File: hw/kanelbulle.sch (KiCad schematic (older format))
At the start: 1 part

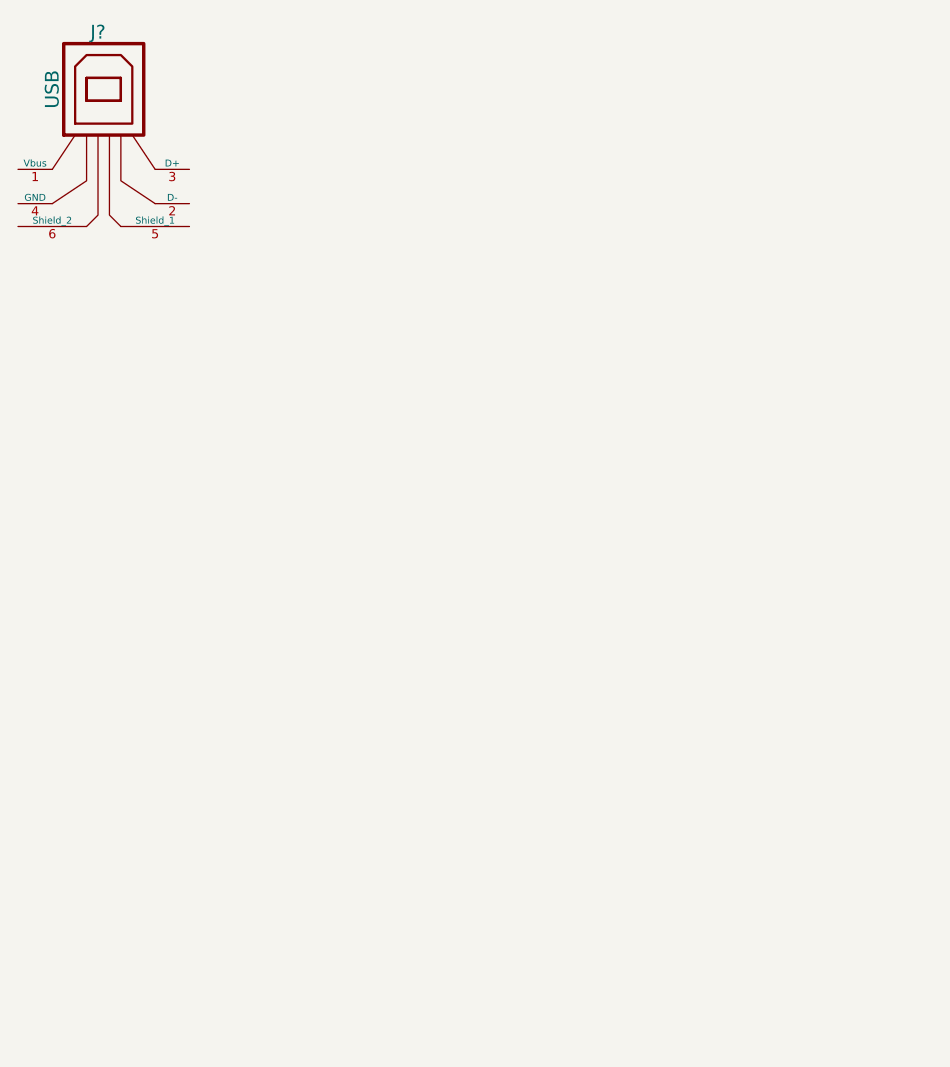
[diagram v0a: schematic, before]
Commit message: added micro controller to schematic
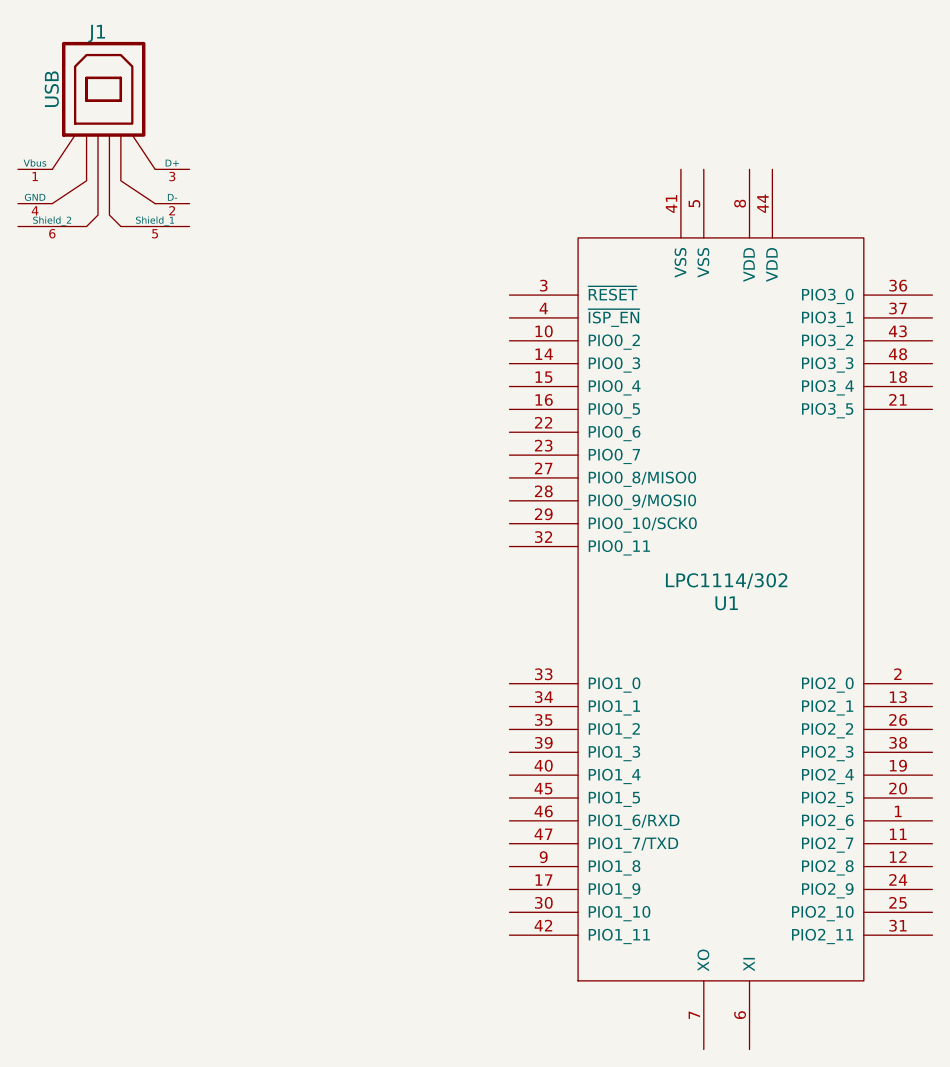
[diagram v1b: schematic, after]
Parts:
- added U1: LPC1114/302, symbol LPC1114/302
- gave numbers to parts that had none: 1
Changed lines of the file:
@@
 LIBS:contrib
 LIBS:valves
+LIBS:LPC1114
+LIBS:kanelbulle-cache
 EELAYER 27 0
 EELAYER END
@@
 $EndDescr
 $Comp
-L USB J?
+L USB J1
 U 1 1 54C8D9E1
 P 3150 1900
-F 0 "J?" H 3100 2300 60  0000 C CNN
+F 0 "J1" H 3100 2300 60  0000 C CNN
 F 1 "USB" V 2900 2050 60  0000 C CNN
 F 2 "" H 3150 1900 60  0000 C CNN
@@
 	1    0    0    -1
 $EndComp
+$Comp
+L LPC1114/302 U1
+U 1 1 54C8DD37
+P 5850 4050
+F 0 "U1" H 5850 4100 60  0000 C CNN
+F 1 "LPC1114/302" H 5850 4200 60  0000 C CNN
+F 2 "" H 5850 4050 60  0000 C CNN
+F 3 "" H 5850 4050 60  0000 C CNN
+	1    5850 4050
+	1    0    0    -1
+$EndComp

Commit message: leds, leds everywhere
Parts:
- added D1, D10, D11, D12, D13, D14, D15, D16, D17, D18, D19, D2, D20, D21, D22, D23, D24, D25, D26, D27, D28, D29, D3, D30, D31, D32, D33, D34, D35, D36, D37, D38, D39, D4, D40, D41, D42, D43, D44, D45, D46, D47, D48, D49, D5, D50, D51, D6, D7, D8, D9: LED_RGB, symbol LED_RGB

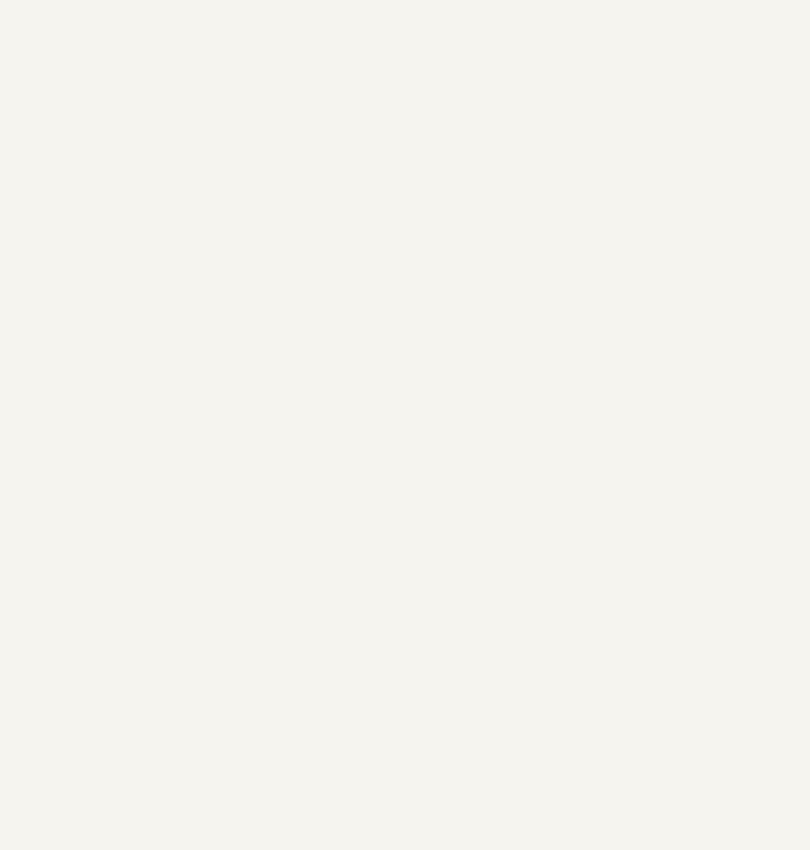
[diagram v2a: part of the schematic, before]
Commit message: added led driver chip
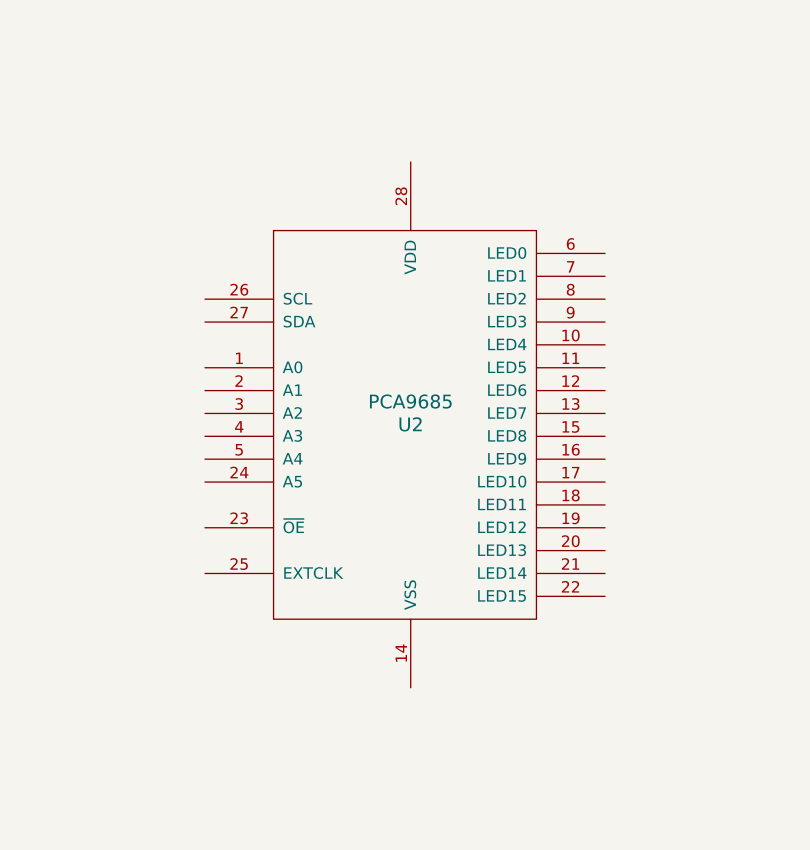
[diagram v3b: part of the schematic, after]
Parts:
- added U2: PCA9685, ~, symbol PCA9685
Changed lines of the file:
@@
 LIBS:LPC1114
 LIBS:led_rgb
+LIBS:pca9685
 LIBS:kanelbulle-cache
 EELAYER 27 0
@@
 	0    -1   -1   0
 $EndComp
+$Comp
+L PCA9685 U2
+U 1 1 54C91061
+P 12950 9250
+F 0 "U2" H 12950 9200 60  0000 C CNN
+F 1 "PCA9685" H 12950 9300 60  0000 C CNN
+F 2 "~" H 13500 8000 60  0000 C CNN
+F 3 "~" H 13500 8000 60  0000 C CNN
+	1    12950 9250
+	1    0    0    -1
+$EndComp
 $EndSCHEMATC

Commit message: connected leds on schematic
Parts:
- added R1, R10, R11, R12, R13, R14, R15, R16, R17, R18, R19, R2, R3, R4, R5, R6, R7, R8, R9: R, ~, symbol R
- added U3, U4, U5: ULN2003A, symbol ULN2003A
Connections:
- net labels added: 3V3, B1, B2, B3, B4, B5, G1, G2, G3, G4, G5, GND, R1, R2, R3, R4, R5, SCL, SDA
- wire segments 0 -> 315
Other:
- moved on the sheet: U2

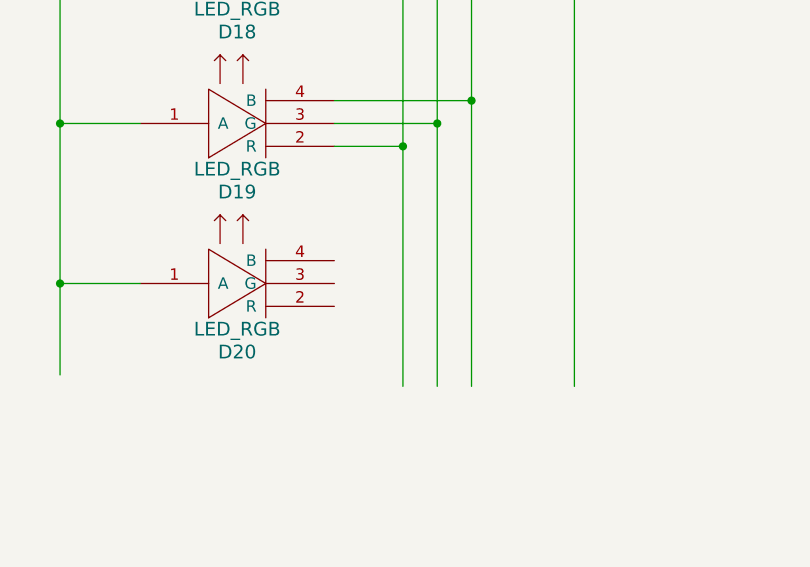
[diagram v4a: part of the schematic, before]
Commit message: connected leds to eachother
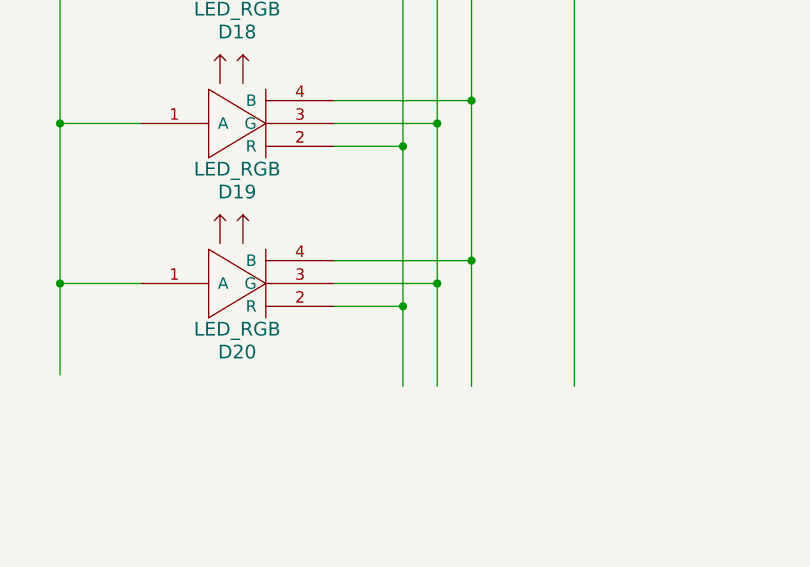
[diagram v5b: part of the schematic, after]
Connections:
- wire segments 315 -> 318
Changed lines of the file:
@@
 Wire Wire Line
 	13900 19200 13750 19200
+Wire Wire Line
+	21300 16400 21900 16400
+Connection ~ 21900 16400
+Wire Wire Line
+	21300 16500 21750 16500
+Connection ~ 21750 16500
+Wire Wire Line
+	21300 16600 21600 16600
+Connection ~ 21600 16600
 $EndSCHEMATC

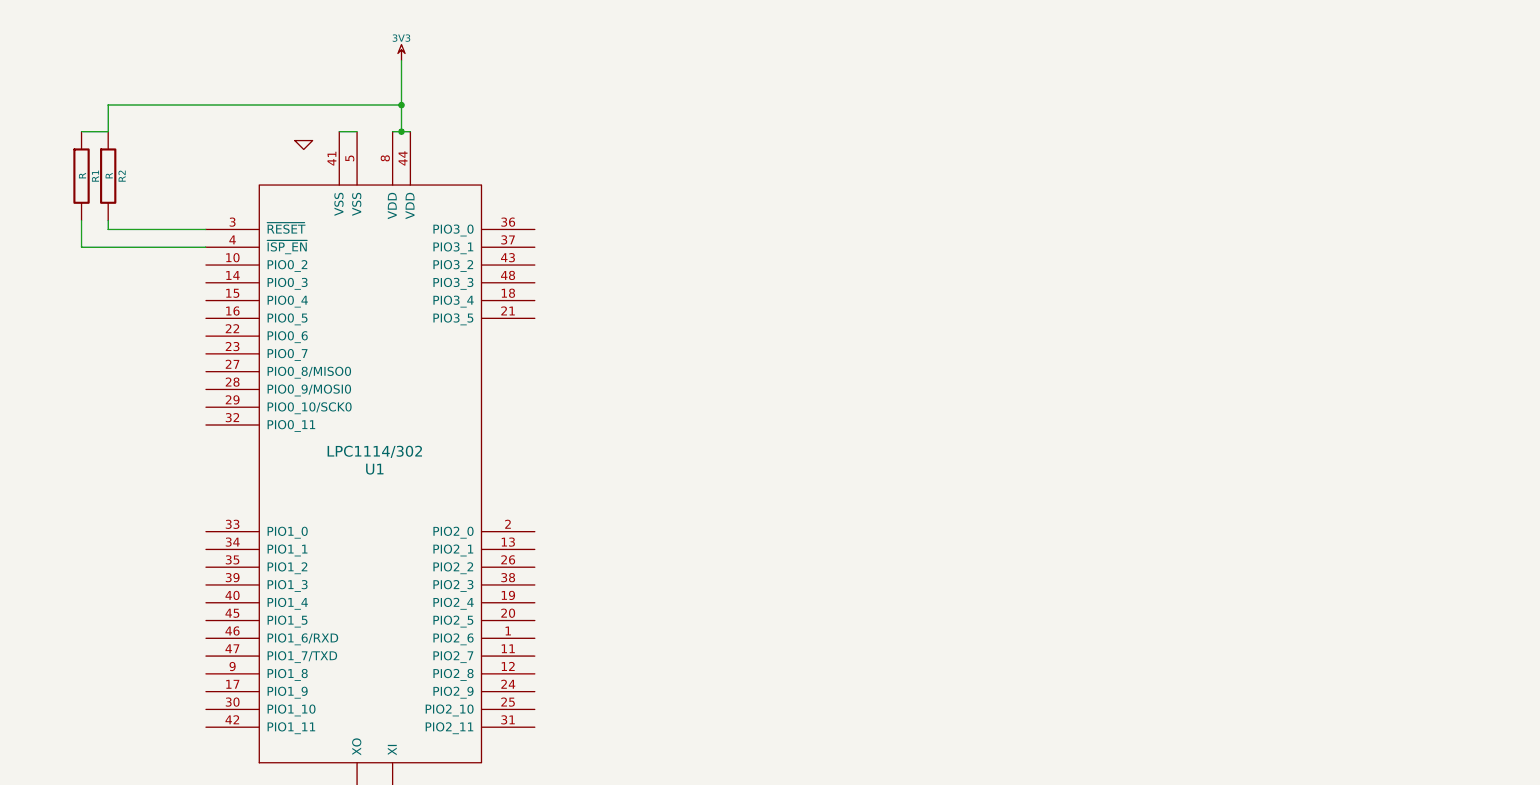
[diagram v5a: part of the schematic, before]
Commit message: connected some OC drivers
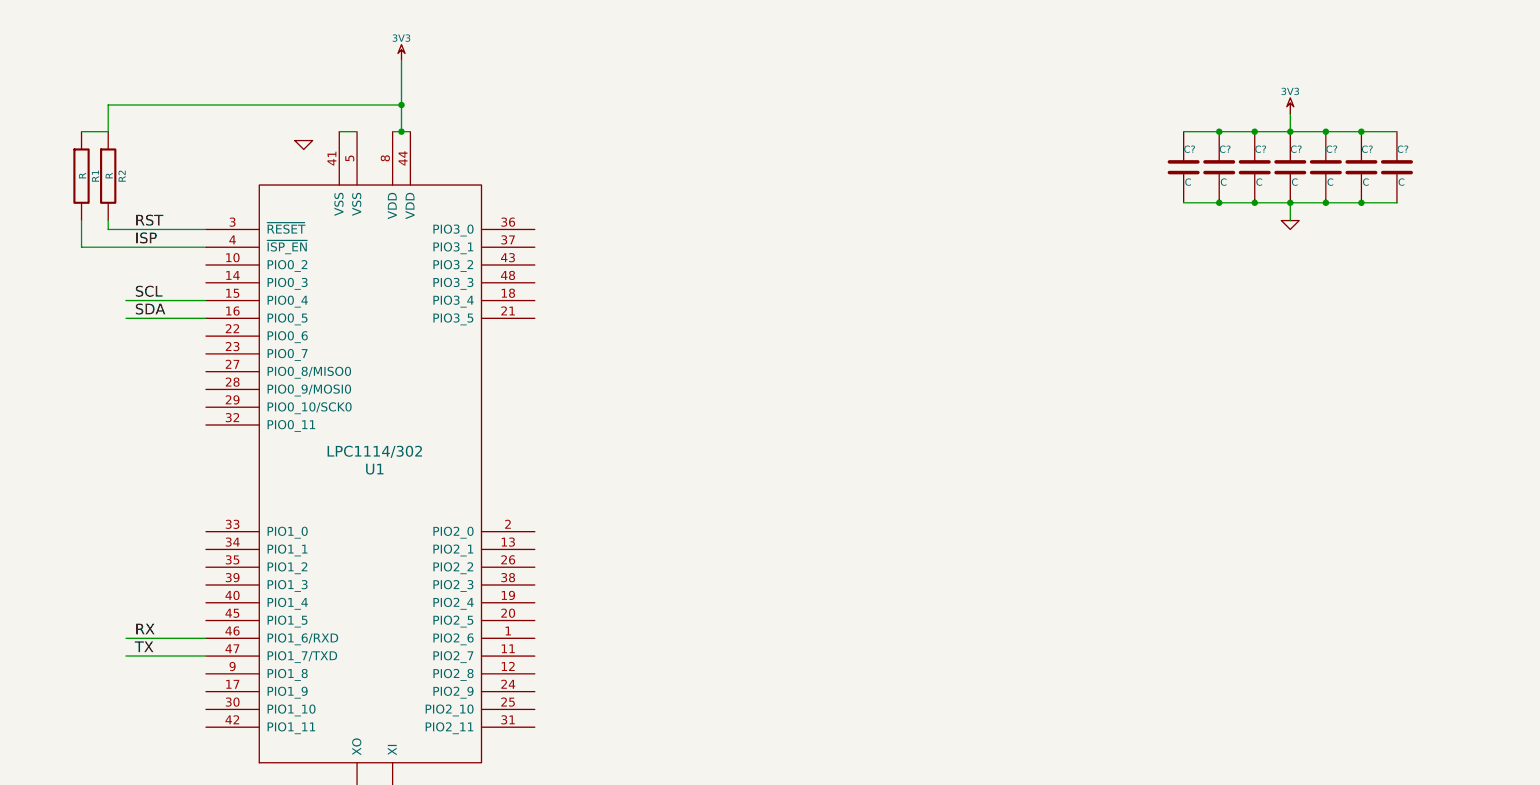
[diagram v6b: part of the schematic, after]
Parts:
- added C? (x7): C, ~, symbol C
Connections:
- net labels added: ISP, RST, RX, TX
- wire segments 318 -> 326
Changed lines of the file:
@@
 	11700 18500 10600 18500
 $Comp
-L 3V3 #PWR5
+L 3V3 #PWR01
 U 1 1 54CFB406
 P 20100 2350
-F 0 "#PWR5" H 20100 2450 40  0001 C CNN
+F 0 "#PWR01" H 20100 2450 40  0001 C CNN
 F 1 "3V3" H 20100 2475 40  0000 C CNN
 F 2 "" H 20100 2350 60  0000 C CNN
@@
 $EndComp
 $Comp
-L 3V3 #PWR6
+L 3V3 #PWR02
 U 1 1 54CFB413
 P 22350 2350
-F 0 "#PWR6" H 22350 2450 40  0001 C CNN
+F 0 "#PWR02" H 22350 2450 40  0001 C CNN
 F 1 "3V3" H 22350 2475 40  0000 C CNN
 F 2 "" H 22350 2350 60  0000 C CNN
@@
 $EndComp
 $Comp
-L 3V3 #PWR7
+L 3V3 #PWR03
 U 1 1 54CFB419
 P 24250 2350
-F 0 "#PWR7" H 24250 2450 40  0001 C CNN
+F 0 "#PWR03" H 24250 2450 40  0001 C CNN
 F 1 "3V3" H 24250 2475 40  0000 C CNN
 F 2 "" H 24250 2350 60  0000 C CNN
@@
 $EndComp
 $Comp
-L 3V3 #PWR8
+L 3V3 #PWR04
 U 1 1 54CFB41F
 P 26100 2350
-F 0 "#PWR8" H 26100 2450 40  0001 C CNN
+F 0 "#PWR04" H 26100 2450 40  0001 C CNN
 F 1 "3V3" H 26100 2475 40  0000 C CNN
 F 2 "" H 26100 2350 60  0000 C CNN
@@
 $EndComp
 $Comp
-L 3V3 #PWR9
+L 3V3 #PWR05
 U 1 1 54CFB425
 P 28050 2350
-F 0 "#PWR9" H 28050 2450 40  0001 C CNN
+F 0 "#PWR05" H 28050 2450 40  0001 C CNN
 F 1 "3V3" H 28050 2475 40  0000 C CNN
 F 2 "" H 28050 2350 60  0000 C CNN
@@
 Connection ~ 8150 16800
 $Comp
-L 3V3 #PWR3
+L 3V3 #PWR06
 U 1 1 54CFC851
 P 8150 16650
-F 0 "#PWR3" H 8150 16750 40  0001 C CNN
+F 0 "#PWR06" H 8150 16750 40  0001 C CNN
 F 1 "3V3" H 8150 16775 40  0000 C CNN
 F 2 "" H 8150 16650 60  0000 C CNN
@@
 $EndComp
 $Comp
-L GND #PWR4
+L GND #PWR07
 U 1 1 54CFC924
 P 8750 19100
-F 0 "#PWR4" H 8750 19100 30  0001 C CNN
+F 0 "#PWR07" H 8750 19100 30  0001 C CNN
 F 1 "GND" H 8750 19030 30  0001 C CNN
 F 2 "" H 8750 19100 60  0000 C CNN
@@
 	5950 2100 6050 2100
 $Comp
-L GND #PWR1
+L GND #PWR08
 U 1 1 54CFDFE0
 P 5450 2150
-F 0 "#PWR1" H 5450 2150 30  0001 C CNN
+F 0 "#PWR08" H 5450 2150 30  0001 C CNN
 F 1 "GND" H 5450 2080 30  0001 C CNN
 F 2 "" H 5450 2150 60  0000 C CNN
@@
 $EndComp
 $Comp
-L 3V3 #PWR2
+L 3V3 #PWR09
 U 1 1 54CFDFEF
 P 6000 1700
-F 0 "#PWR2" H 6000 1800 40  0001 C CNN
+F 0 "#PWR09" H 6000 1800 40  0001 C CNN
 F 1 "3V3" H 6000 1825 40  0000 C CNN
 F 2 "" H 6000 1700 60  0000 C CNN
@@
 	21300 16600 21600 16600
 Connection ~ 21600 16600
+Wire Wire Line
+	4900 3050 4450 3050
+Wire Wire Line
+	4900 3150 4450 3150
+Text Label 4500 3050 0    60   ~ 0
+SCL
+Text Label 4500 3150 0    60   ~ 0
+SDA
+Text Label 4500 2650 0    60   ~ 0
+RST
+Text Label 4500 2750 0    60   ~ 0
+ISP
+Wire Wire Line
+	4900 4950 4450 4950
+Wire Wire Line
+	4900 5050 4450 5050
+Text Label 4500 4950 0    60   ~ 0
+RX
+Text Label 4500 5050 0    60   ~ 0
+TX
+$Comp
+L C C?
+U 1 1 54CFB5F9
+P 10600 2300
+F 0 "C?" H 10600 2400 40  0000 L CNN
+F 1 "C" H 10606 2215 40  0000 L CNN
+F 2 "~" H 10638 2150 30  0000 C CNN
+F 3 "~" H 10600 2300 60  0000 C CNN
+	1    10600 2300
+	1    0    0    -1
+$EndComp
+$Comp
+L C C?
+U 1 1 54CFB606
+P 10800 2300
+F 0 "C?" H 10800 2400 40  0000 L CNN
+F 1 "C" H 10806 2215 40  0000 L CNN
+F 2 "~" H 10838 2150 30  0000 C CNN
+F 3 "~" H 10800 2300 60  0000 C CNN
+	1    10800 2300
+	1    0    0    -1
+$EndComp
+$Comp
+L C C?
+U 1 1 54CFB60C
+P 11000 2300
+F 0 "C?" H 11000 2400 40  0000 L CNN
+F 1 "C" H 11006 2215 40  0000 L CNN
+F 2 "~" H 11038 2150 30  0000 C CNN
+F 3 "~" H 11000 2300 60  0000 C CNN
+	1    11000 2300
+	1    0    0    -1
+$EndComp
+$Comp
+L C C?
+U 1 1 54CFB612
+P 11200 2300
+F 0 "C?" H 11200 2400 40  0000 L CNN
+F 1 "C" H 11206 2215 40  0000 L CNN
+F 2 "~" H 11238 2150 30  0000 C CNN
+F 3 "~" H 11200 2300 60  0000 C CNN
+	1    11200 2300
+	1    0    0    -1
+$EndComp
+$Comp
+L C C?
+U 1 1 54CFB618
+P 11400 2300
+F 0 "C?" H 11400 2400 40  0000 L CNN
+F 1 "C" H 11406 2215 40  0000 L CNN
+F 2 "~" H 11438 2150 30  0000 C CNN
+F 3 "~" H 11400 2300 60  0000 C CNN
+	1    11400 2300
+	1    0    0    -1
+$EndComp
+$Comp
+L C C?
+U 1 1 54CFB61E
+P 11600 2300
+F 0 "C?" H 11600 2400 40  0000 L CNN
+F 1 "C" H 11606 2215 40  0000 L CNN
+F 2 "~" H 11638 2150 30  0000 C CNN
+F 3 "~" H 11600 2300 60  0000 C CNN
+	1    11600 2300
+	1    0    0    -1
+$EndComp
+$Comp
+L C C?
+U 1 1 54CFB624
+P 10400 2300
+F 0 "C?" H 10400 2400 40  0000 L CNN
+F 1 "C" H 10406 2215 40  0000 L CNN
+F 2 "~" H 10438 2150 30  0000 C CNN
+F 3 "~" H 10400 2300 60  0000 C CNN
+	1    10400 2300
+	1    0    0    -1
+$EndComp
+Wire Wire Line
+	10400 2100 11600 2100
+Connection ~ 10600 2100
+Connection ~ 10800 2100
+Connection ~ 11000 2100
+Connection ~ 11200 2100
+Connection ~ 11400 2100
+Wire Wire Line
+	10400 2500 11600 2500
+Connection ~ 10600 2500
+Connection ~ 10800 2500
+Connection ~ 11000 2500
+Connection ~ 11200 2500
+Connection ~ 11400 2500
+$Comp
+L GND #PWR?
+U 1 1 54CFCF5E
+P 11000 2600
+F 0 "#PWR?" H 11000 2600 30  0001 C CNN
+F 1 "GND" H 11000 2530 30  0001 C CNN
+F 2 "" H 11000 2600 60  0000 C CNN
+F 3 "" H 11000 2600 60  0000 C CNN
+	1    11000 2600
+	1    0    0    -1
+$EndComp
+Wire Wire Line
+	11000 2600 11000 2500
+$Comp
+L 3V3 #PWR?
+U 1 1 54CFD18D
+P 11000 2000
+F 0 "#PWR?" H 11000 2100 40  0001 C CNN
+F 1 "3V3" H 11000 2125 40  0000 C CNN
+F 2 "" H 11000 2000 60  0000 C CNN
+F 3 "" H 11000 2000 60  0000 C CNN
+	1    11000 2000
+	1    0    0    -1
+$EndComp
+Wire Wire Line
+	11000 2000 11000 2100
 $EndSCHEMATC
